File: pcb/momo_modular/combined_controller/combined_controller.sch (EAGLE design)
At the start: 45 parts, among them Q1 32.768khz, Q2 P-MOSFET, U1 XRP7659, U2 PIC24FJ64GA306, U3 MCP1702, U5 FLASH8MSOP8, U6 MCP73811

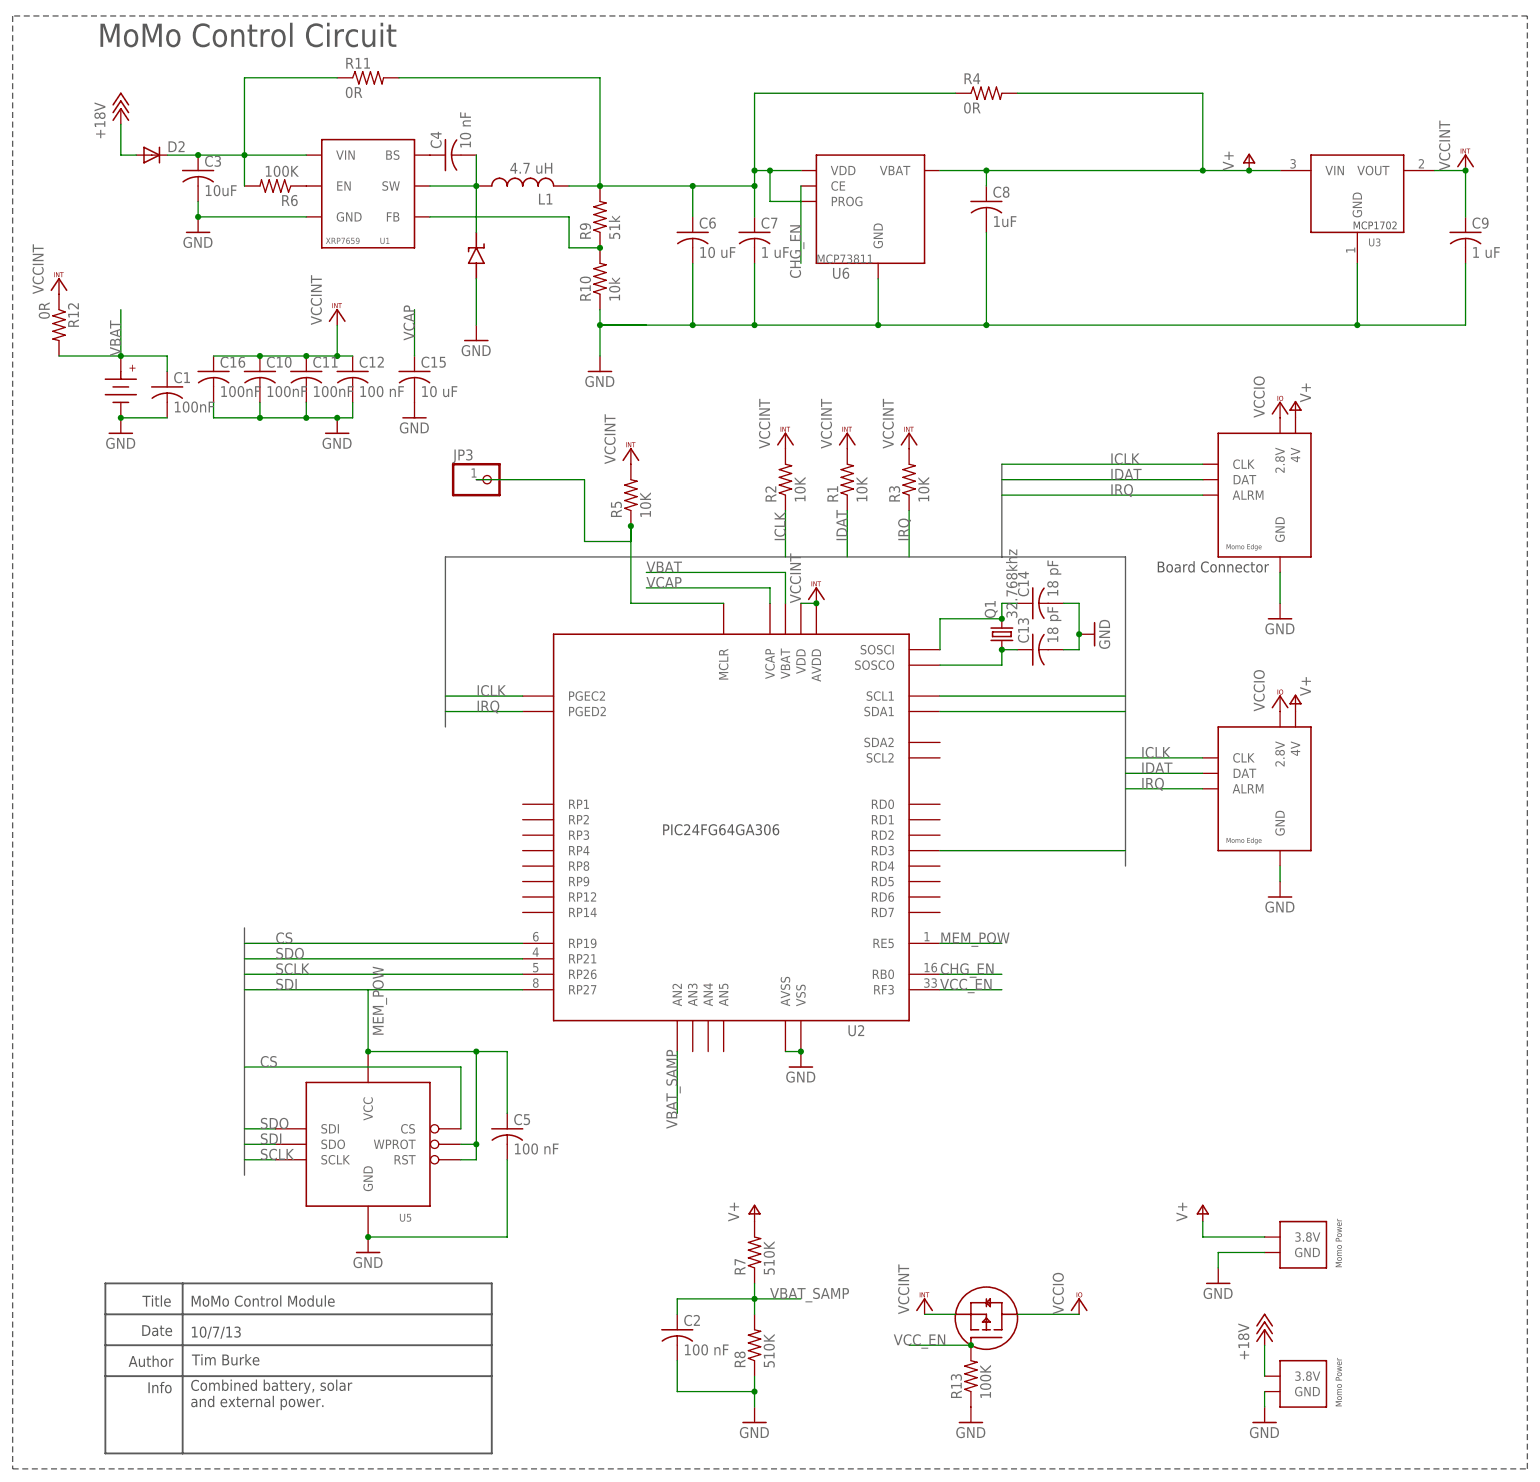
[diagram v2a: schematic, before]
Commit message: Update Controller Board Layout
- add sense line for external power
- move components for easier placement
- reroute long lines
- flip backup battery orientation to allow for easy insertion
- move cap away from crystal to avoid shorts
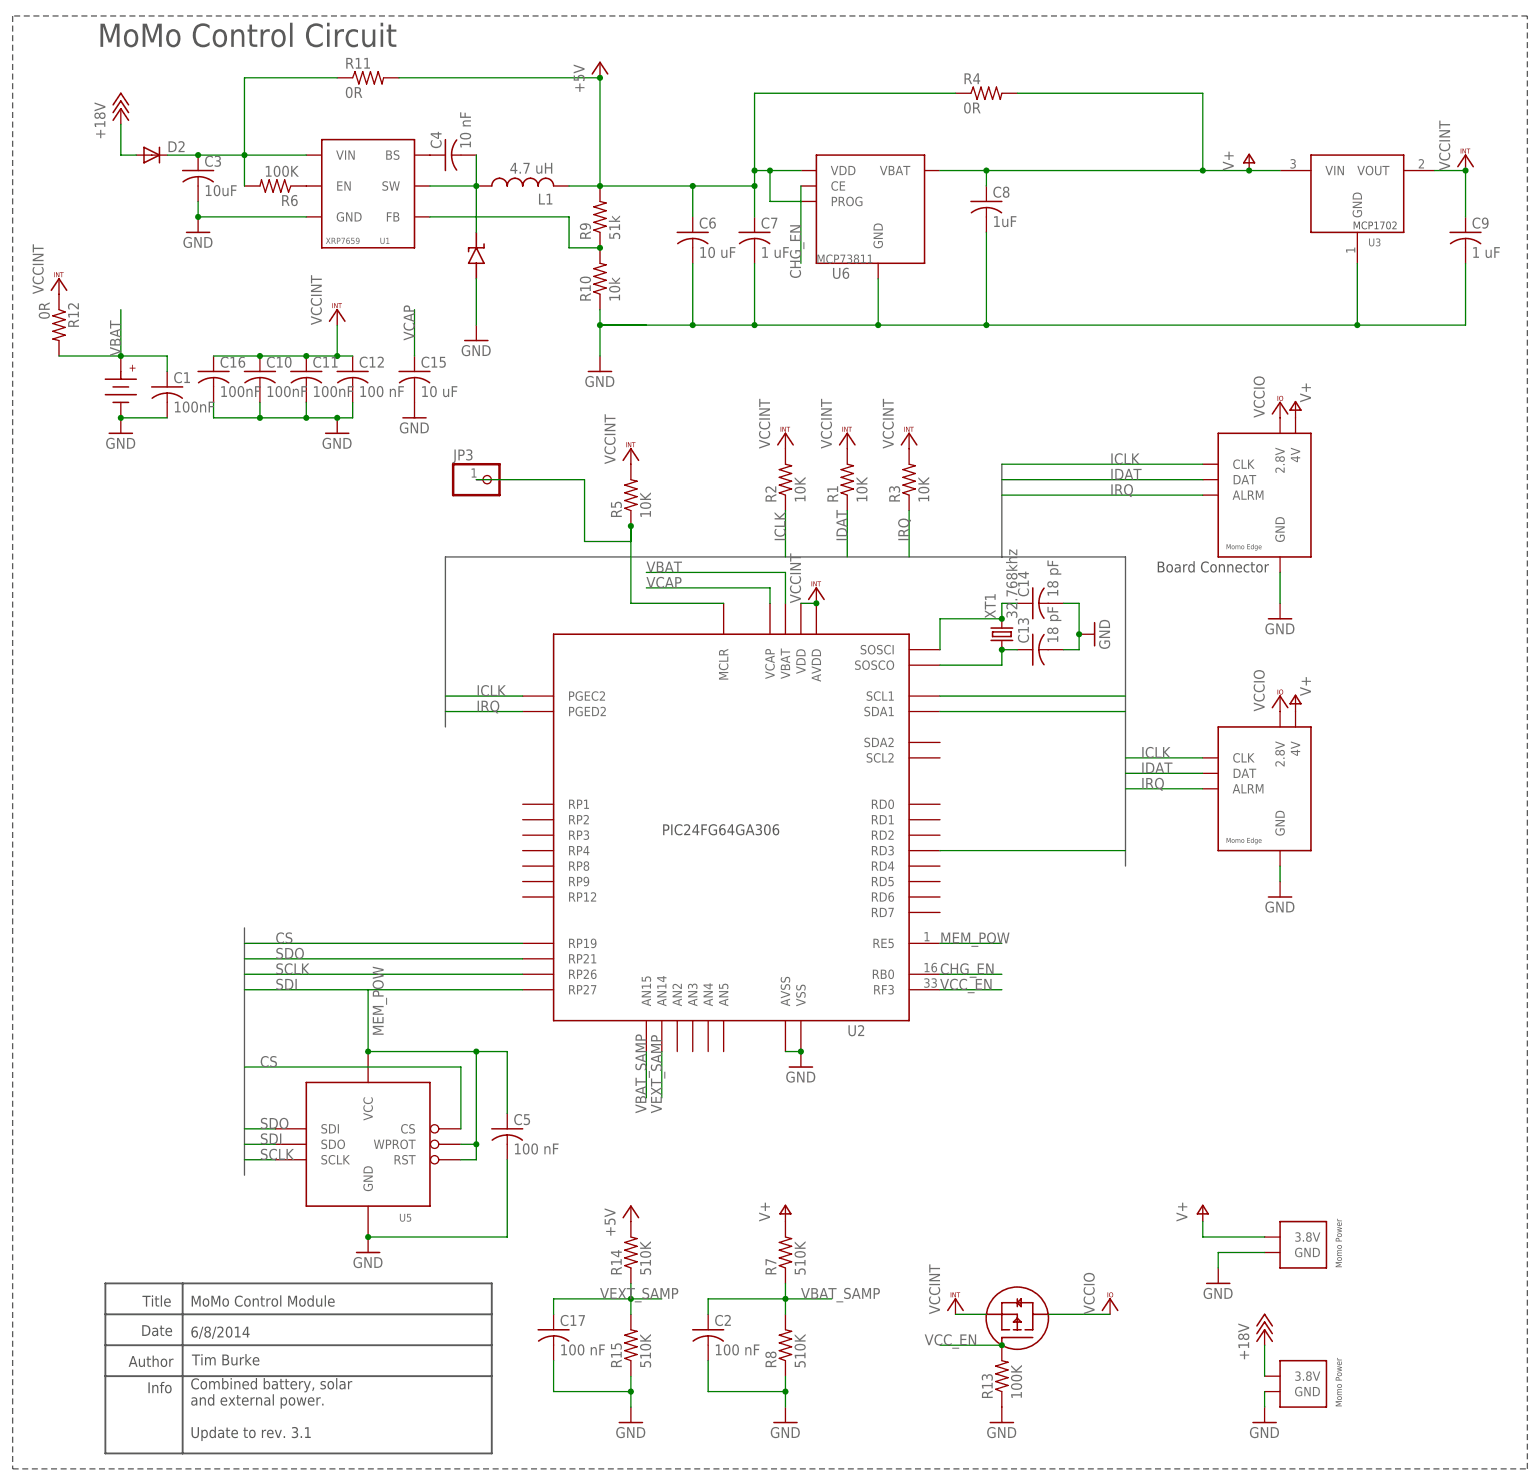
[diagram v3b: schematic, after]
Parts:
- removed Q1: 32.768khz, crystal:CRYSTALTC26H
- added C17: 100 nF, rcl:C-USC0402
- added R14, R15: 510K, rcl:R-US_R0603
- added XT1: 32.768khz, components:XTAL-W-CAN-PAD
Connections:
- removed net N$5: C6.1, C7.1, L1.2, R11.2, R4.1, R9.2, U6.PROG, U6.VDD
- new net +5V: C6.1, C7.1, L1.2, R11.2, R14.2, R4.1, R9.2, U6.PROG, U6.VDD
- new net VEXT_SAMP: C17.1, R14.1, R15.2, U2.AN14
- net GND: now also C17.2, R15.1
- net N$6: now also XT1.2; no longer Q1.2
- net N$7: now also XT1.1; no longer Q1.1
- net VBAT_SAMP: now also U2.AN15; no longer U2.AN2
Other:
- note added: "6/8/2014"
- note added: "Combined battery, solar and external power. Update to rev. 3.1"
- note removed: "10/7/13"
- note removed: "Combined battery, solar and external power."
- moved on the sheet: C2, R13, R7, R8
